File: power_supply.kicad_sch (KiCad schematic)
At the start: 37 parts, among them CON1 USB_B_Micro, CON2 Barrel_Jack_MountingPin, Q1 AO3401A, U1 AP1117-33, U3 CP2102N

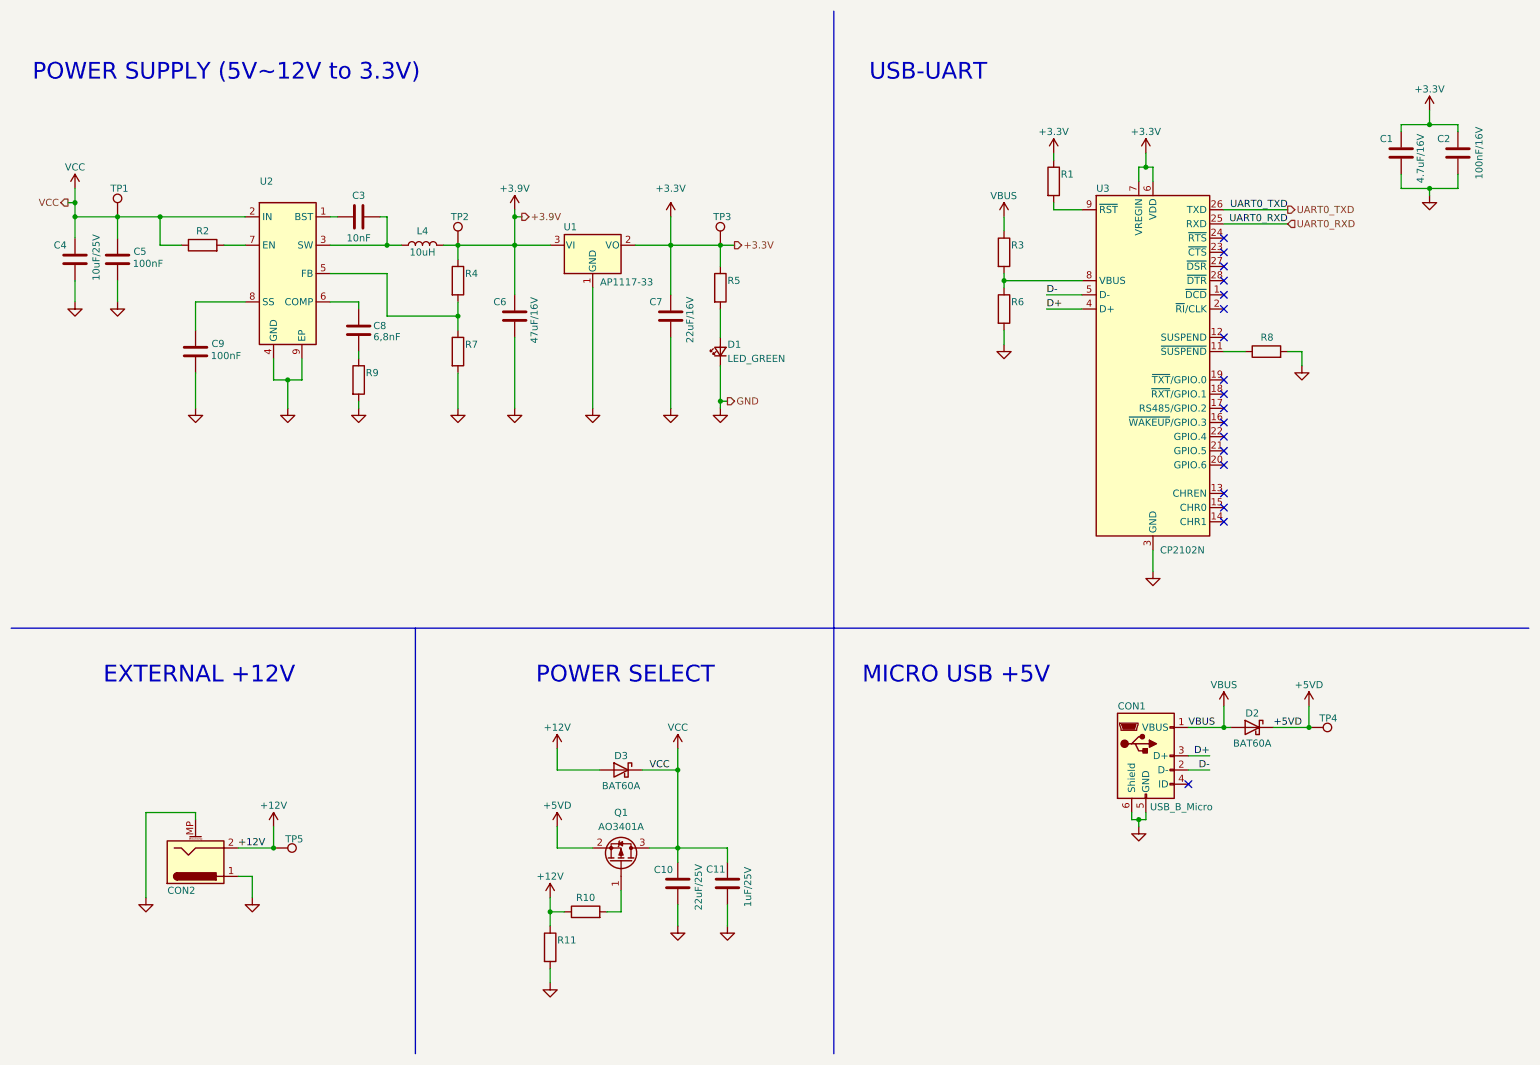
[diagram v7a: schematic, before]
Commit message: Atualização das referências dos componentes
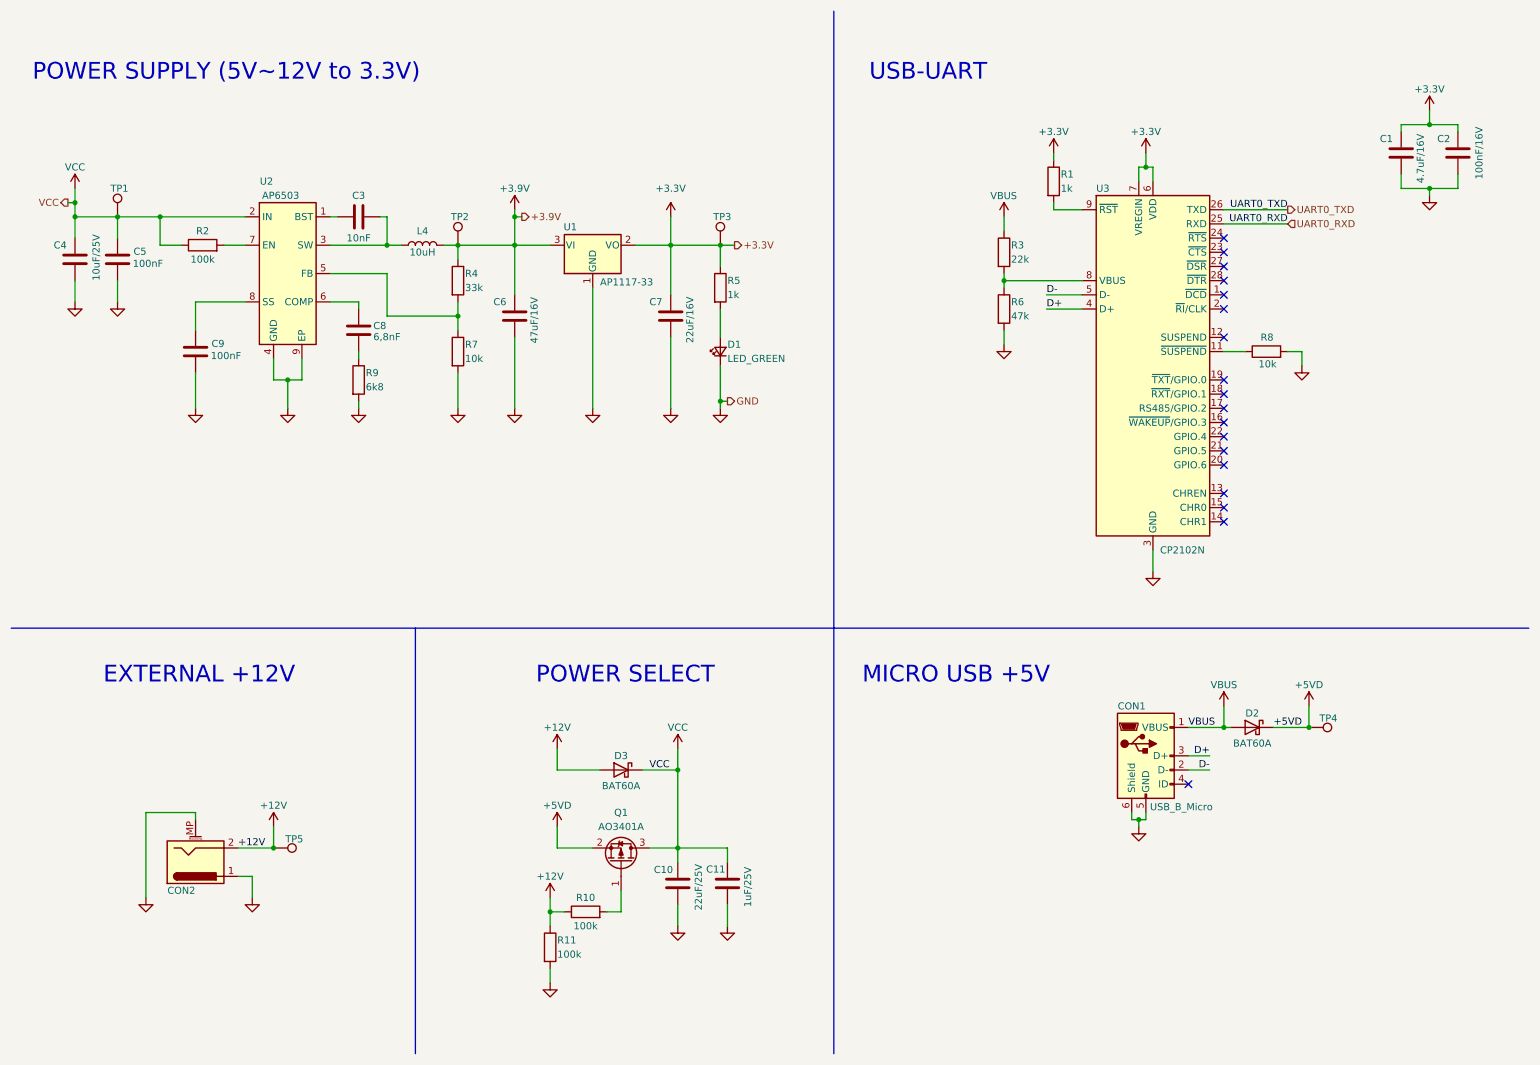
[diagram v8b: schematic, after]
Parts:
- R1, R5: value (none) -> 1k; footprint (none) -> Resistor_SMD:R_0603_1608Metric_Pad0.98x0.95mm_HandSolder
- R10, R11, R2: value (none) -> 100k; footprint (none) -> Resistor_SMD:R_0603_1608Metric_Pad0.98x0.95mm_HandSolder
- R3: value (none) -> 22k; footprint (none) -> Resistor_SMD:R_0603_1608Metric_Pad0.98x0.95mm_HandSolder
- R4: value (none) -> 33k; footprint (none) -> Resistor_SMD:R_0603_1608Metric_Pad0.98x0.95mm_HandSolder
- R6: value (none) -> 47k; footprint (none) -> Resistor_SMD:R_0603_1608Metric_Pad0.98x0.95mm_HandSolder
- R7, R8: value (none) -> 10k; footprint (none) -> Resistor_SMD:R_0603_1608Metric_Pad0.98x0.95mm_HandSolder
- R9: value (none) -> 6k8; footprint (none) -> Resistor_SMD:R_0603_1608Metric_Pad0.98x0.95mm_HandSolder
- TP1: value (none) -> TestPoint
- U2: value (none) -> AP6503; footprint (none) -> Package_SO:SOIC-8-1EP_3.9x4.9mm_P1.27mm_EP2.41x3.81mm_ThermalVias
